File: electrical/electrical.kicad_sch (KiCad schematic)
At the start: 0 parts

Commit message: Interim check-in
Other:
- added sheet Lycoming (lycoming.kicad_sch)
- sheet Multifunction ports: added SMOKE_PWR; removed none
- sheet Power ports: added IGN_BAK_LOW, IGN_BAK_VOLTS, IGN_PWR, SMOKE_PWR; removed BAK_BATTERY_VOLTS
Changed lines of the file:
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@@
 	(title_block
 		(title "Electrical Overview")
-		(date "2024-05-21")
-		(rev "1.0.3")
+		(date "2025-11-01")
+		(rev "1.1")
 		(company "N877RV")
 	)
 	(text_box "Canbus Order\nGMU11\nGSA28 Yaw\nGSA28 Pitch\nG5\nGDU460\nGSU25\nGTR20\nGMC507\nGAD29\nGEA24\nGAD27\nGSA28 Roll"
 		(exclude_from_sim no)
-		(at 16.51 16.51 0)
+		(at 18.034 13.462 0)
 		(size 19.05 27.94)
 		(margins 0.9525 0.9525 0.9525 0.9525)
@@
 		)
 	)
+	(text_box "Standard Colors\n\nCanbus\nHi: White\nLo: White/Blue\n\nSerial\nTx: White\nRx: White/Blue\nGnd: White/Orange\n\nAudio\nLeft: White\nRight: White/Blue\nLo: White/Orange"
+		(exclude_from_sim no)
+		(at 39.37 187.198 0)
+		(size 34.29 51.054)
+		(margins 0.9525 0.9525 0.9525 0.9525)
+		(stroke
+			(width 0)
+			(type solid)
+		)
+		(fill
+			(type none)
+		)
+		(effects
+			(font
+				(size 1.27 1.27)
+			)
+			(justify left top)
+		)
+	)
 	(junction
 		(at 298.45 123.19)
@@
 	(wire
 		(pts
-			(xy 91.44 55.88) (xy 182.88 55.88)
+			(xy 46.99 55.88) (xy 52.07 55.88)
 		)
 		(stroke
@@
 	(wire
 		(pts
-			(xy 355.6 55.88) (xy 364.49 55.88)
+			(xy 91.44 55.88) (xy 182.88 55.88)
 		)
 		(stroke
@@
 	(wire
 		(pts
-			(xy 166.37 181.61) (xy 166.37 114.3)
+			(xy 355.6 55.88) (xy 364.49 55.88)
 		)
 		(stroke
@@
 	(wire
 		(pts
-			(xy 259.08 162.56) (xy 309.88 162.56)
+			(xy 166.37 181.61) (xy 166.37 114.3)
 		)
 		(stroke
@@
 	(wire
 		(pts
-			(xy 52.07 106.68) (xy 45.72 106.68)
+			(xy 259.08 162.56) (xy 309.88 162.56)
 		)
 		(stroke
@@
 	(wire
 		(pts
-			(xy 308.61 72.39) (xy 298.45 72.39)
+			(xy 52.07 106.68) (xy 45.72 106.68)
 		)
 		(stroke
@@
 	(wire
 		(pts
-			(xy 47.625 109.22) (xy 47.625 123.825)
+			(xy 308.61 72.39) (xy 298.45 72.39)
 		)
 		(stroke
@@
 	(wire
 		(pts
-			(xy 45.72 126.365) (xy 50.8 126.365)
+			(xy 45.72 123.19) (xy 50.8 123.19)
 		)
 		(stroke
@@
 	(wire
 		(pts
-			(xy 45.72 106.68) (xy 45.72 126.365)
+			(xy 45.72 106.68) (xy 45.72 123.19)
 		)
 		(stroke
@@
 	(wire
 		(pts
+			(xy 20.32 142.24) (xy 20.32 66.04)
+		)
+		(stroke
+			(width 0)
+			(type default)
+		)
+	)
+	(wire
+		(pts
 			(xy 355.6 64.77) (xy 388.62 64.77)
 		)
@@
 	(wire
 		(pts
+			(xy 50.8 142.24) (xy 20.32 142.24)
+		)
+		(stroke
+			(width 0)
+			(type default)
+		)
+	)
+	(wire
+		(pts
 			(xy 355.6 48.26) (xy 364.49 48.26)
 		)
@@
 	(wire
 		(pts
+			(xy 17.78 167.64) (xy 105.41 167.64)
+		)
+		(stroke
+			(width 0)
+			(type default)
+		)
+	)
+	(wire
+		(pts
 			(xy 304.8 127) (xy 304.8 167.64)
 		)
@@
 	(wire
 		(pts
+			(xy 46.99 62.23) (xy 52.07 62.23)
+		)
+		(stroke
+			(width 0)
+			(type default)
+		)
+	)
+	(wire
+		(pts
 			(xy 196.85 199.39) (xy 200.66 199.39)
 		)
@@
 	(wire
 		(pts
+			(xy 20.32 66.04) (xy 22.352 66.04)
+		)
+		(stroke
+			(width 0)
+			(type default)
+		)
+	)
+	(wire
+		(pts
 			(xy 102.87 189.23) (xy 105.41 189.23)
 		)
@@
 	(wire
 		(pts
-			(xy 52.07 109.22) (xy 47.625 109.22)
+			(xy 46.99 58.42) (xy 52.07 58.42)
 		)
 		(stroke
@@
 	(wire
 		(pts
+			(xy 13.97 168.91) (xy 17.78 168.91)
+		)
+		(stroke
+			(width 0)
+			(type default)
+		)
+	)
+	(wire
+		(pts
 			(xy 298.45 123.19) (xy 308.61 123.19)
 		)
@@
 	(wire
 		(pts
+			(xy 13.97 50.8) (xy 52.07 50.8)
+		)
+		(stroke
+			(width 0)
+			(type default)
+		)
+	)
+	(wire
+		(pts
 			(xy 292.1 140.97) (xy 95.25 140.97)
 		)
@@
 	(wire
 		(pts
+			(xy 13.97 50.8) (xy 13.97 168.91)
+		)
+		(stroke
+			(width 0)
+			(type default)
+		)
+	)
+	(wire
+		(pts
 			(xy 308.61 116.84) (xy 292.1 116.84)
 		)
@@
 	(wire
 		(pts
-			(xy 47.625 123.825) (xy 50.8 123.825)
+			(xy 367.03 196.85) (xy 367.03 127)
 		)
 		(stroke
@@
 	(wire
 		(pts
-			(xy 367.03 196.85) (xy 367.03 127)
+			(xy 17.78 168.91) (xy 17.78 167.64)
 		)
 		(stroke
@@
 			)
 		)
-		(pin "BAK_BATTERY_VOLTS" output
-			(at 52.07 109.22 180)
-			(effects
-				(font
-					(size 1.27 1.27)
-				)
-				(justify left)
-			)
-		)
 		(pin "GMC507_PWR" output
 			(at 91.44 101.6 0)
@@
 		)
 		(pin "AIRCRAFT_PWR" input
-			(at 52.07 48.26 180)
+			(at 52.07 55.88 180)
 			(effects
 				(font
@@
 		)
 		(pin "AIRCRAFT_GROUND" input
-			(at 52.07 50.8 180)
+			(at 52.07 58.42 180)
 			(effects
 				(font
@@
 			)
 		)
+		(pin "IGN_BAK_LOW" output
+			(at 52.07 85.09 180)
+			(effects
+				(font
+					(size 1.27 1.27)
+				)
+				(justify left)
+			)
+		)
+		(pin "IGN_BAK_VOLTS" output
+			(at 52.07 87.63 180)
+			(effects
+				(font
+					(size 1.27 1.27)
+				)
+				(justify left)
+			)
+		)
+		(pin "IGN_PWR" output
+			(at 52.07 62.23 180)
+			(effects
+				(font
+					(size 1.27 1.27)
+				)
+				(justify left)
+			)
+		)
+		(pin "SMOKE_PWR" output
+			(at 52.07 50.8 180)
+			(effects
+				(font
+					(size 1.27 1.27)
+				)
+				(justify left)
+			)
+		)
 		(instances
 			(project "electrical"
@@
 			)
 		)
+		(pin "SMOKE_PWR" input
+			(at 105.41 167.64 180)
+			(effects
+				(font
+					(size 1.27 1.27)
+				)
+				(justify left)
+			)
+		)
 		(instances
 			(project "electrical"
@@
 		)
 		(pin "BAK_BATTERY_VOLTS" input
-			(at 50.8 123.825 180)
+			(at 50.8 142.24 180)
 			(effects
 				(font
@@
 		)
 		(pin "FUEL_ON" input
-			(at 50.8 126.365 180)
+			(at 50.8 123.19 180)
 			(effects
 				(font
@@
 				)
 			)
+		)
+	)
+	(sheet
+		(at 22.352 54.61)
+		(size 24.638 13.97)
+		(exclude_from_sim no)
+		(in_bom yes)
+		(on_board yes)
+		(dnp no)
+		(fields_autoplaced yes)
+		(stroke
+			(width 0.1524)
+			(type solid)
+		)
+		(fill
+			(color 0 0 0 0.0000)
+		)
+		(property "Sheetname" "Lycoming"
+			(at 22.352 53.8984 0)
+			(effects
+				(font
+					(size 1.27 1.27)
+				)
+				(justify left bottom)
+			)
+		)
+		(property "Sheetfile" "lycoming.kicad_sch"
+			(at 22.352 69.1646 0)
+			(effects
+				(font
+					(size 1.27 1.27)
+				)
+				(justify left top)
+			)
+		)
+		(pin "AIRCRAFT_GND" passive
+			(at 46.99 58.42 0)
+			(effects
+				(font
+					(size 1.27 1.27)
+				)
+				(justify right)
+			)
+		)
+		(pin "AIRCRAFT_PWR" output
+			(at 46.99 55.88 0)
+			(effects
+				(font
+					(size 1.27 1.27)
+				)
+				(justify right)
+			)
+		)
+		(pin "BAK_BATTERY_VOLTS" output
+			(at 22.352 66.04 180)
+			(effects
+				(font
+					(size 1.27 1.27)
+				)
+				(justify left)
+			)
+		)
+		(pin "IGN_PWR" input
+			(at 46.99 62.23 0)
+			(effects
+				(font
+					(size 1.27 1.27)
+				)
+				(justify right)
+			)
+		)
+		(instances
+			(project "electrical"
+				(path "/e8ec215a-dbe2-4eba-a577-e50a0a128049"
+					(page "3")
+				)
+			)

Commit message: Went through and changed a lot from discussions and tradeoffs. Added GTX 330, rmemoved Connext from GDU and added to GPS 175 from GDL 52. Added relay for smoke and to not use GAD 27. Added Tach sensor for SureFly. Added carb heat. Added connectors to run panel disconnected.
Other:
- removed sheet Miscellaneous
- sheet Autopilot ports: added CAN_HI_YAW_OUT, CAN_LO_YAW_OUT, CWS_ON, PITCH_TRIM1, PITCH_TRIM2, PITCH_TRIM_HI, PITCH_TRIM_LO, PITCH_TRIM_POS; removed CAN_HI_PITCH_OUT, CAN_HI_YAW_IN, CAN_LO_PITCH_OUT, CAN_LO_YAW_IN
- sheet Communication ports: added PILOT_PTT; removed none
- sheet EIS ports: added AMPS_HI, AMPS_LO, GEA24_PWR_2, IGN_BAK_LOW, IGN_BAK_VOLTS, L_PLEAD, PITCH_TRIM_HI, PITCH_TRIM_LO, PITCH_TRIM_POS, R_PLEAD; removed GEA24_BAK_PWR
- sheet Lycoming ports: added AMPS_HI, AMPS_LO, BAK_BAT_WARN, L_PLEAD, R_PLEAD; removed none
- sheet Multifunction ports: added CWS_ON, EARTHX_IN, FUEL_PUMP_ON, GDU4XX_PWR_2, GEA24_PWR_2, GMU11_PWR_2, GSU25_PWR_2, KEEP_PWR, LANDING_LT, LANDING_RT, PILOT_PTT, PITCH_TRIM1, PITCH_TRIM2, SMOKE_LT, SMOKE_SW, TRIM_PWR; removed none
- sheet Navigator ports: added TXPDR_SERIAL_GND, TXPDR_SERIAL_IN, TXPDR_SERIAL_OUT; removed CONNEXT_SERIAL_GND, CONNEXT_SERIAL_IN, CONNEXT_SERIAL_OUT
- sheet PFD ports: added AIRDATA_SERIAL_IN, CANBUS_GDU_HI_OUT, CANBUS_GDU_LO_OUT, CANBUS_HI_GMU_IN, CANBUS_LO_GMU_IN, ELT_PWR, GDU4XX_PWR_2, GMU11_PWR_2, GSU25_PWR_2; removed CANBUS_HI_GMU_OUT, CANBUS_HI_IN, CANBUS_HI_OUT, CANBUS_LO_GMU_OUT, CANBUS_LO_IN, CANBUS_LO_OUT, ELT_SERIAL_GND, ELT_SERIAL_OUT, NAV_CONNEXT_SERIAL_GND, NAV_CONNEXT_SERIAL_IN, NAV_CONNEXT_SERIAL_OUT, XPDR_AIRDATA_SERIAL_GND, XPDR_AIRDATA_SERIAL_IN, XPDR_AIRDATA_SERIAL_OUT
- sheet Power ports: added FUEL_PUMP_ON, GTX330_PWR, KEEP_PWR, LANDING_LT, LANDING_RT, LIGHT_PWR, SMOKE_LT, SMOKE_SW, TRIM_PWR; removed ENCODER_PWR, GTX320_PWR, LAND_TAXI_PWR, TAILBCN_PWR
- sheet Transponder ports: added AIRDATA_RS232_OUT, GPS_RS232_GND, GPS_RS232_IN, GPS_RS232_OUT, GTX330_PWR; removed AIRDATA_SERIAL_GND, AIRDATA_SERIAL_IN, AIRDATA_SERIAL_OUT, ENCODER_PWR, GTX320_PWR

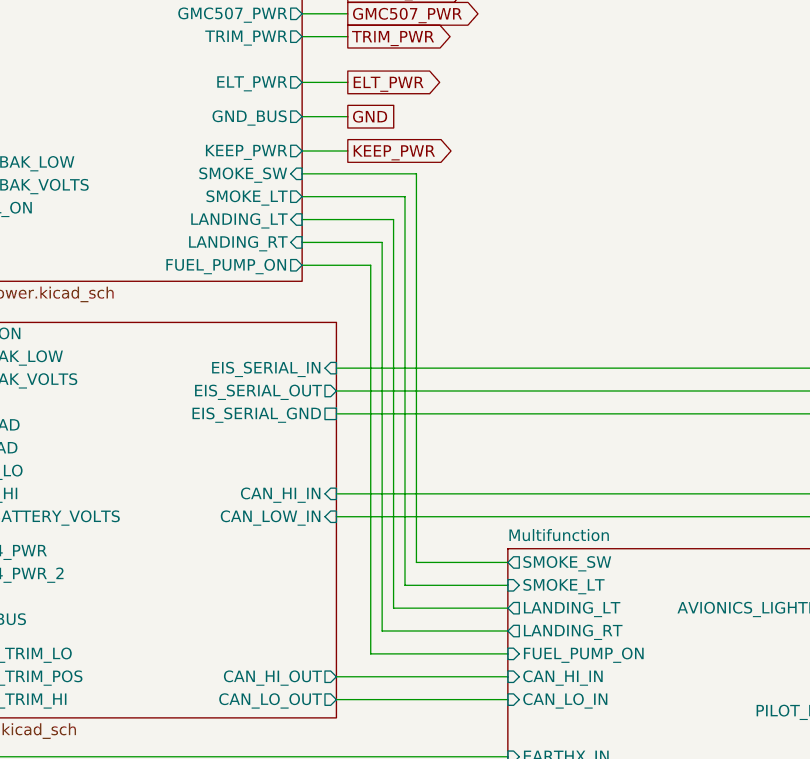
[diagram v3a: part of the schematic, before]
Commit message: Added extra connector for GDL 52, rewired stick to have flaps up/down instead of level/smoke. Put smoke on panel.
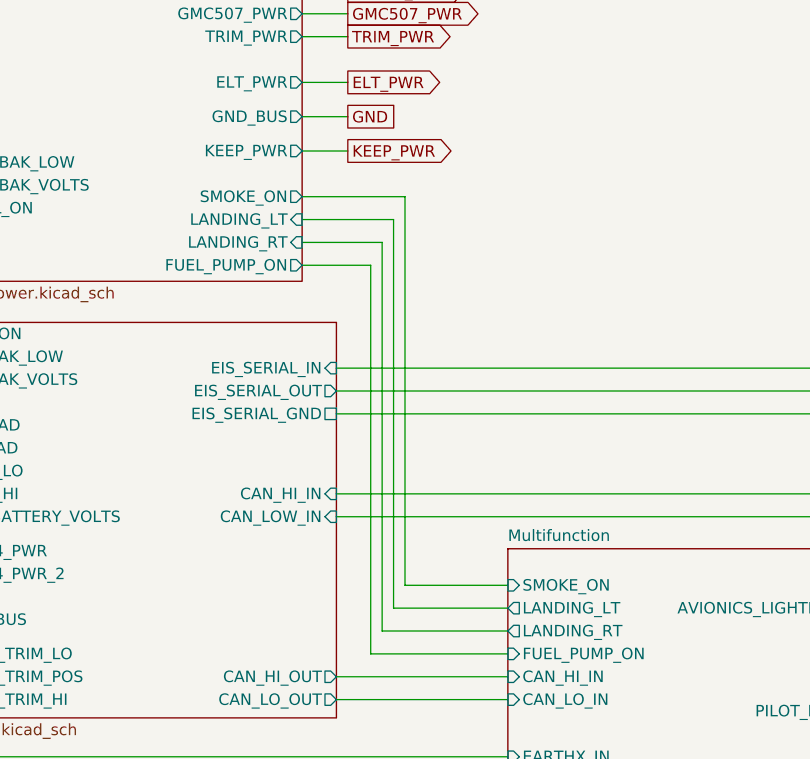
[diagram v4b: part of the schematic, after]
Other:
- sheet Multifunction ports: added SMOKE_ON; removed SMOKE_LT, SMOKE_SW
- sheet Power ports: added SMOKE_ON; removed SMOKE_LT, SMOKE_SW
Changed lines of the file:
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@@
 	(title_block
 		(title "Electrical Overview")
-		(date "2025-12-24")
-		(rev "1.2")
+		(date "2025-12-31")
+		(rev "1.2.2")
 		(company "N877RV")
 	)
@@
 	(wire
 		(pts
-			(xy 128.27 148.59) (xy 118.11 148.59)
-		)
-		(stroke
-			(width 0)
-			(type default)
-		)
-	)
-	(wire
-		(pts
 			(xy 64.77 135.89) (xy 33.02 135.89)
 		)
@@
 	(wire
 		(pts
-			(xy 118.11 105.41) (xy 105.41 105.41)
-		)
-		(stroke
-			(width 0)
-			(type default)
-		)
-	)
-	(wire
-		(pts
 			(xy 273.05 162.56) (xy 323.85 162.56)
 		)
@@
 	(wire
 		(pts
-			(xy 118.11 148.59) (xy 118.11 105.41)
-		)
-		(stroke
-			(width 0)
-			(type default)
-		)
-	)
-	(wire
-		(pts
 			(xy 62.738 63.5) (xy 66.04 63.5)
 		)
@@
 			)
 		)
-		(pin "SMOKE_LT" output
+		(pin "SMOKE_ON" output
 			(at 105.41 107.95 0)
 			(effects
@@
 			)
 		)
-		(pin "SMOKE_SW" input
-			(at 105.41 105.41 0)
-			(effects
-				(font
-					(size 1.27 1.27)
-				)
-				(justify right)
-			)
-		)
 		(instances
 			(project "electrical"
@@
 			)
 		)
-		(pin "SMOKE_LT" input
+		(pin "SMOKE_ON" input
 			(at 128.27 151.13 180)
 			(effects
 				(font
-					(size 1.27 1.27)
-				)
-				(justify left)
-			)
-		)
-		(pin "SMOKE_SW" output
-			(at 128.27 148.59 180)
-			(effects
-				(font

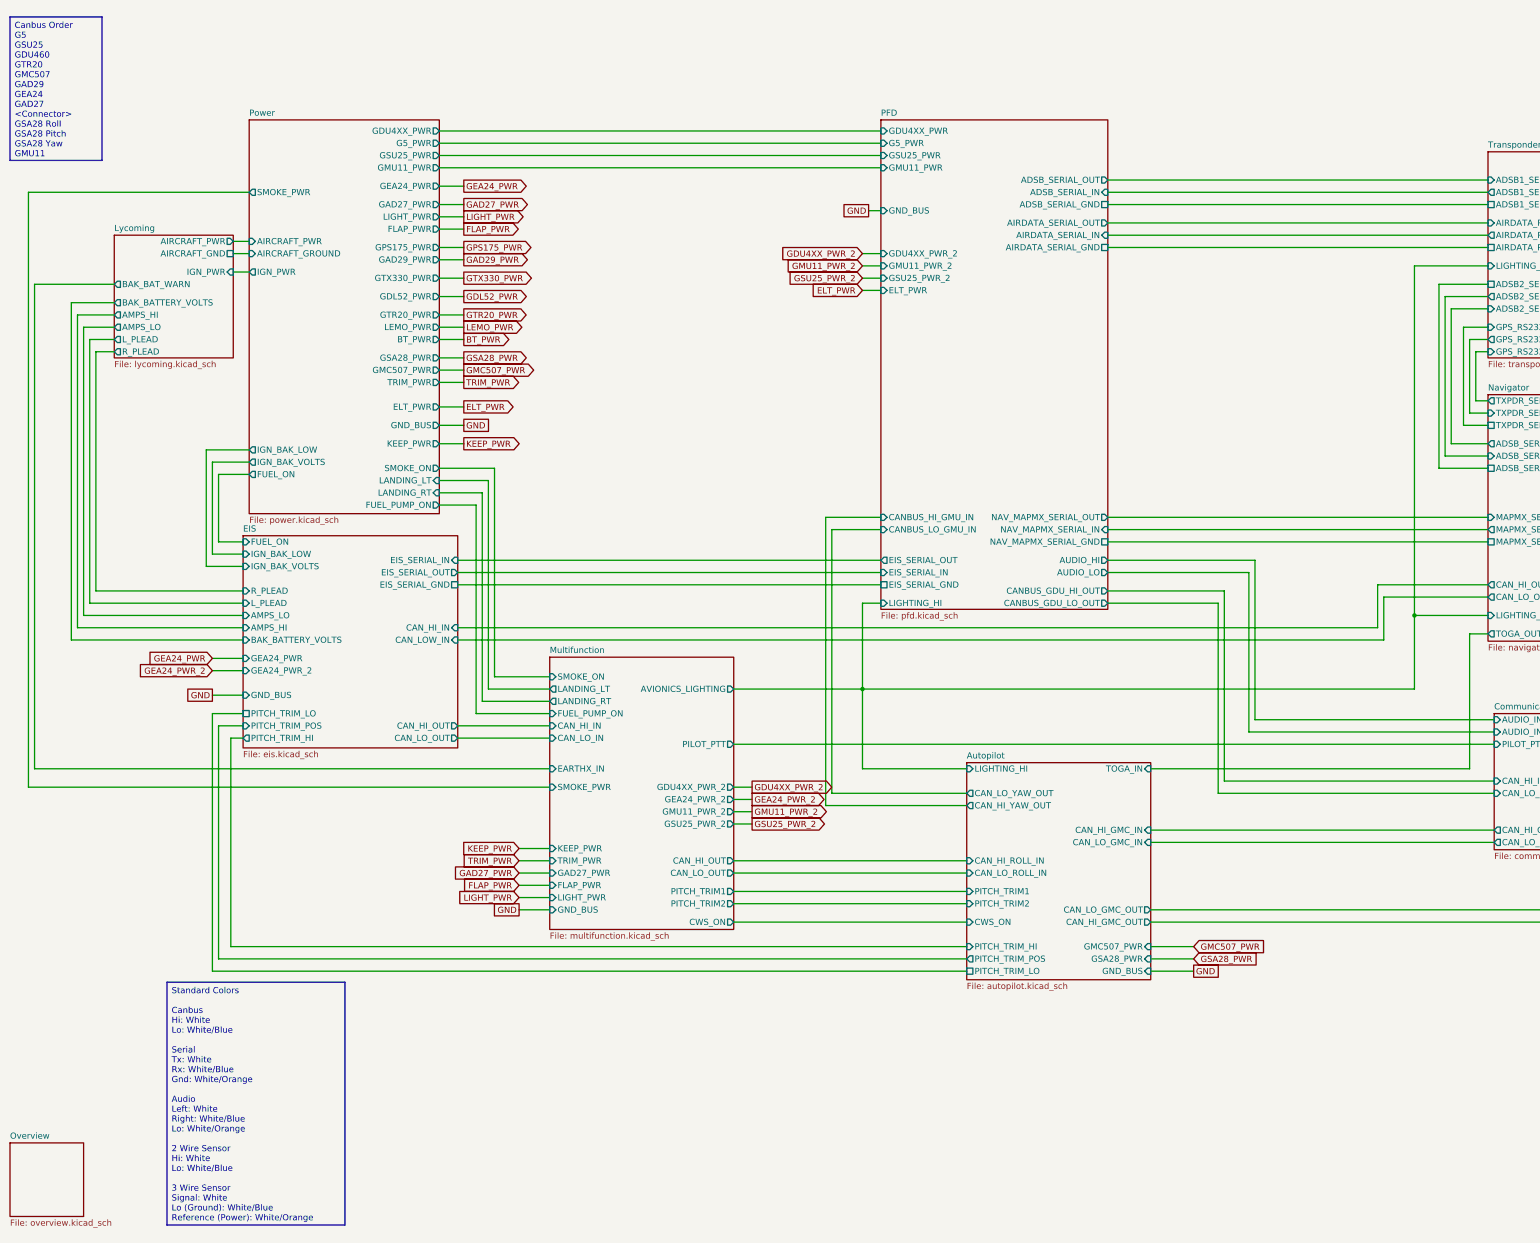
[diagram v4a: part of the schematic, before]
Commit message: Added light power
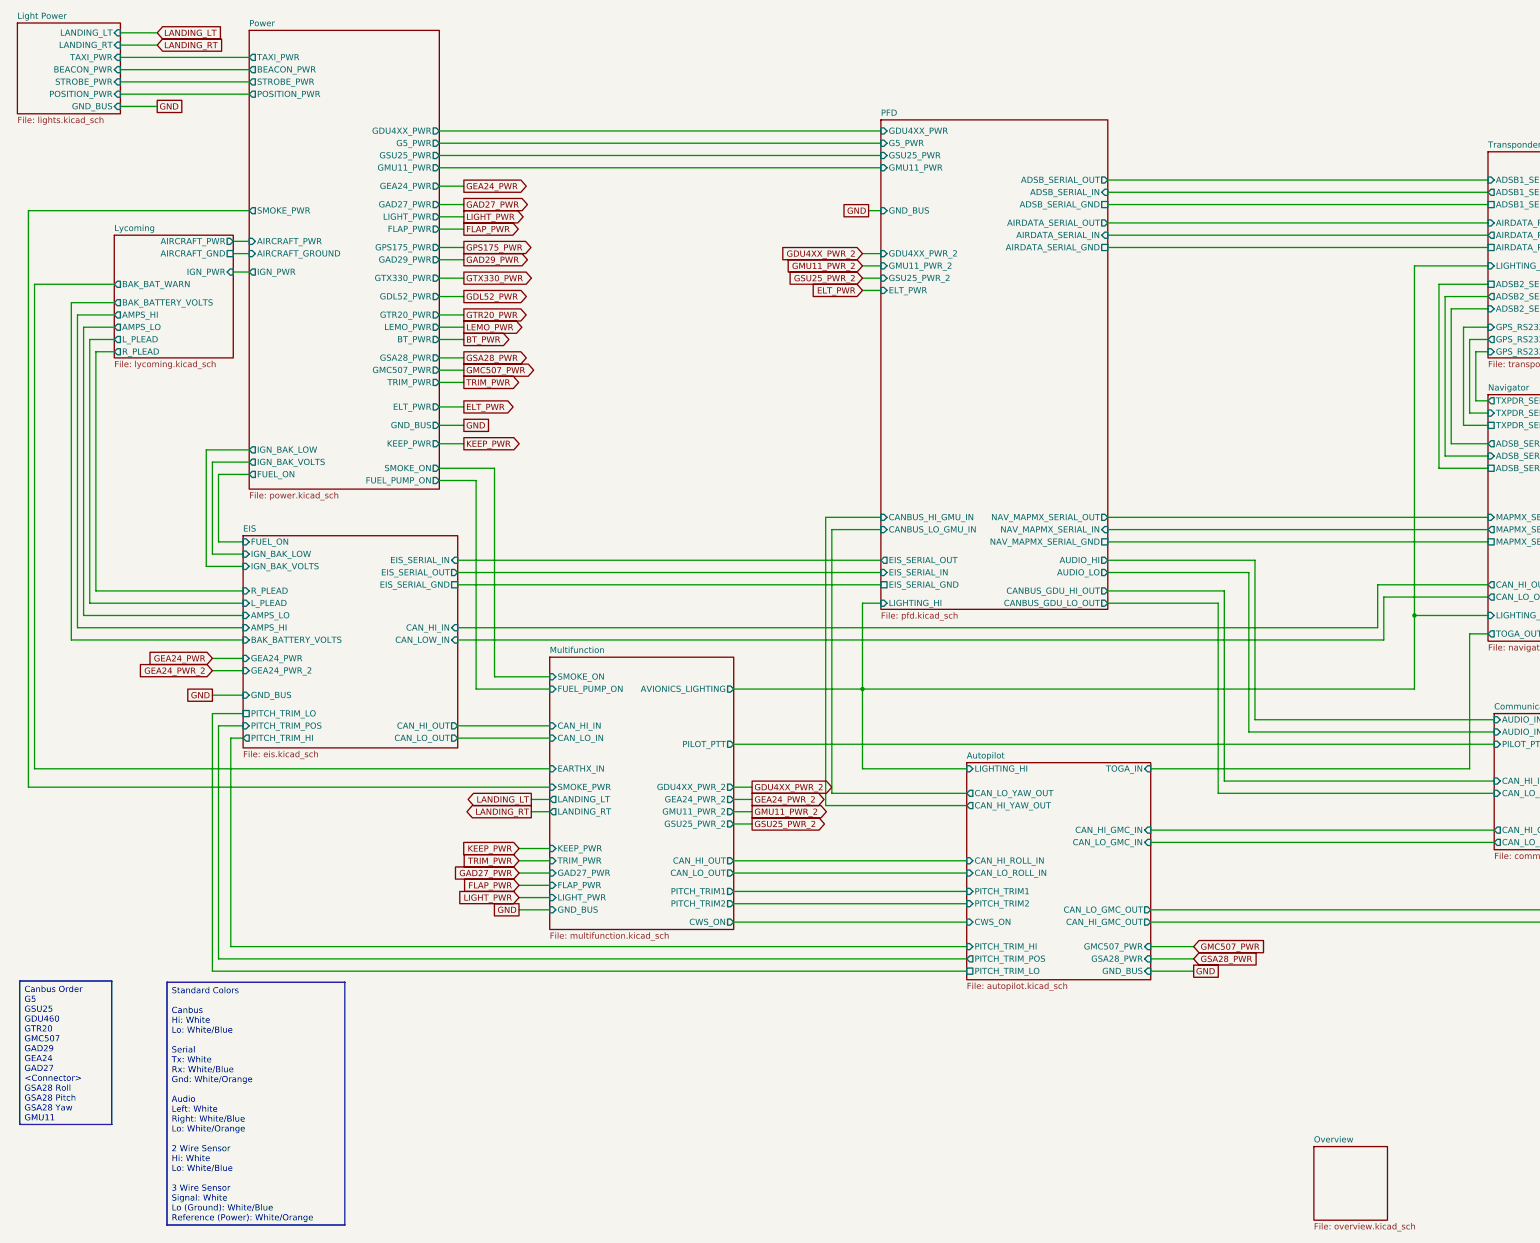
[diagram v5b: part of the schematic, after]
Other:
- added sheet Light Power (lights.kicad_sch)
- sheet Power ports: added BEACON_PWR, POSITION_PWR, STROBE_PWR, TAXI_PWR; removed LANDING_LT, LANDING_RT
